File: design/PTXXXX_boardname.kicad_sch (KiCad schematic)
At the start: 14 parts

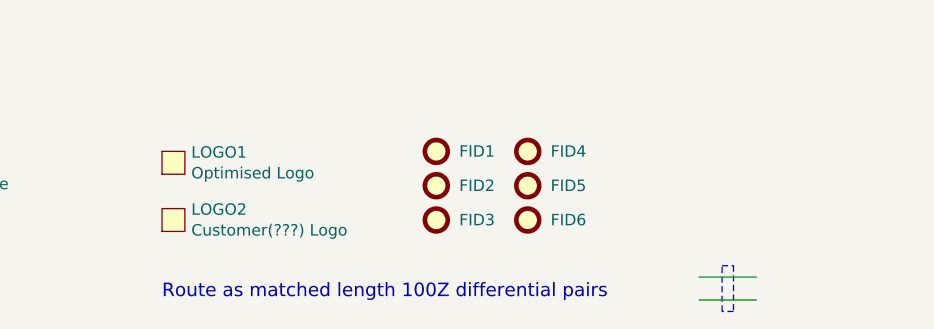
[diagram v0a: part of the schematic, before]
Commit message: added 90Z_DIFF net class to template updated template to use net directive set diff pair highlight colour to light blue/cyan
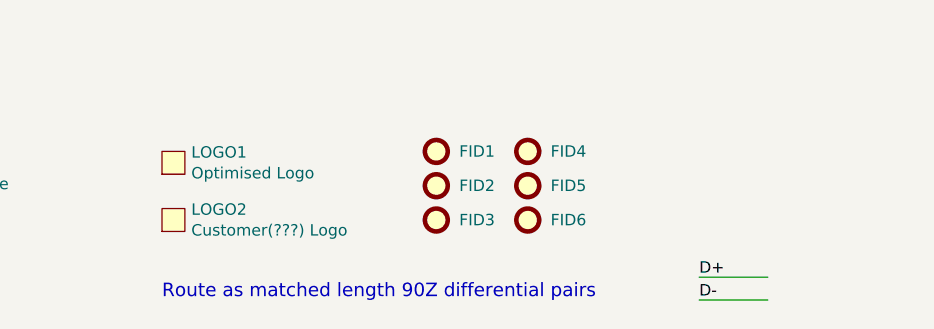
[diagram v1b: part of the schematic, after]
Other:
- note added: "Route as matched length 90Z differential pairs"
- note removed: "Route as matched length 100Z differential pairs"
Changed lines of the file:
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@@
-		)
-	)
-	(rectangle
-		(start 163.83 186.69)
-		(end 165.1 191.77)
-		(stroke
-			(width 0)
-			(type dash_dot_dot)
-		)
-		(fill
-			(type none)
 		)
 	)
@@
 		)
 	)
-	(text "Route as matched length 100Z differential pairs"
+	(text "Route as matched length 90Z differential pairs"
 		(exclude_from_sim no)
 		(at 101.6 190.5 0)
@@
 	(wire
 		(pts
-			(xy 161.29 190.5) (xy 167.64 190.5)
+			(xy 161.29 190.5) (xy 168.91 190.5)
 		)
 		(stroke
@@
 	(wire
 		(pts
-			(xy 161.29 187.96) (xy 167.64 187.96)
+			(xy 161.29 187.96) (xy 168.91 187.96)
 		)
 		(stroke
@@
 				)
 			)
+		)
+	)
+	(label "D+"
+		(at 161.29 187.96 0)
+		(effects
+			(font
+				(size 1.27 1.27)
+			)
+			(justify left bottom)
+		)
+	)
+	(label "D-"
+		(at 161.29 190.5 0)
+		(effects
+			(font
+				(size 1.27 1.27)
+			)
+			(justify left bottom)
+		)
+	)
+	(rule_area
+		(polyline
+			(pts
+				(xy 165.1 186.69) (xy 165.1 191.77) (xy 166.37 191.77) (xy 166.37 186.69)
+			)
+			(stroke
+				(width 0)
+				(type dash)
+			)
+			(fill
+				(type none)
+			)
+		)
+	)
+	(netclass_flag ""
+		(length 1.27)
+		(shape round)
+		(at 165.735 186.69 0)
+		(fields_autoplaced yes)
+		(effects
+			(font
+				(size 1.27 1.27)
+			)
+			(justify left bottom)
+		)
+		(property "Netclass" "90Z_DIFF"
+			(at 166.3446 185.42 0)
+			(effects
+				(font
+					(size 0.635 0.635)
+					(thickness 0.127)
+					(bold yes)
+				)
+				(justify left)
+			)
+		)
+		(property "Component Class" ""
+			(at -43.18 21.59 0)
+			(effects
+				(font
+					(size 1.27 1.27)
+					(italic yes)
+				)
+			)
